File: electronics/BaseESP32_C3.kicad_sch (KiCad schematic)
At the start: 21 parts, among them J10 Conn_01x06, J11 Boot jumper, SW1 SW_Push, U1 ESP32-C3-MINI-1-N4

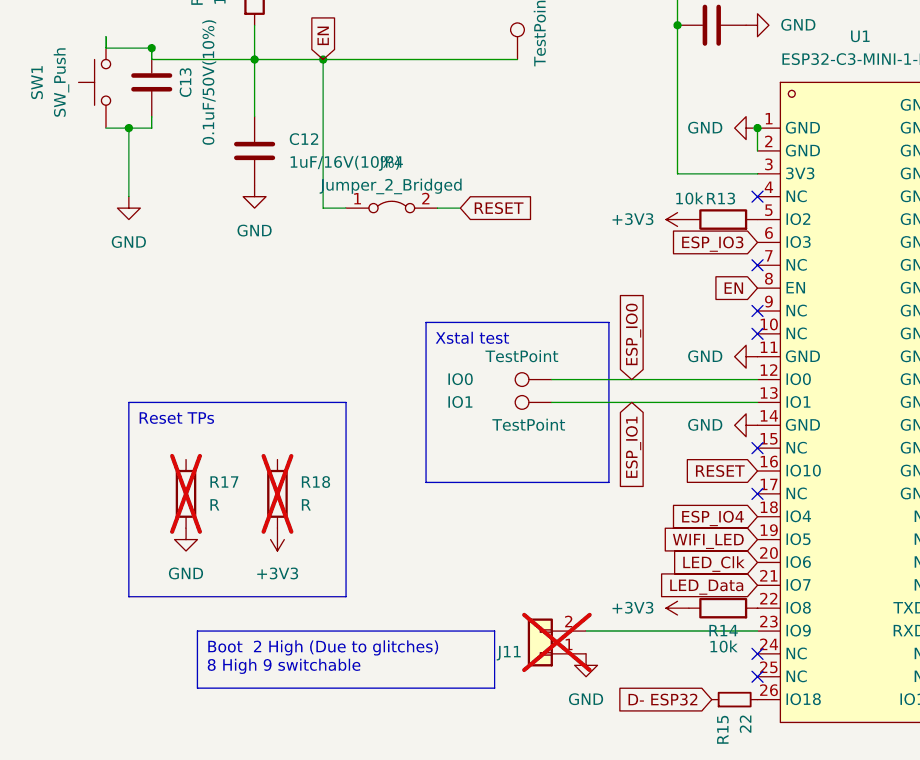
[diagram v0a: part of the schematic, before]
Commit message: components placed and tracks routed, needs silkscreen, drc and checking
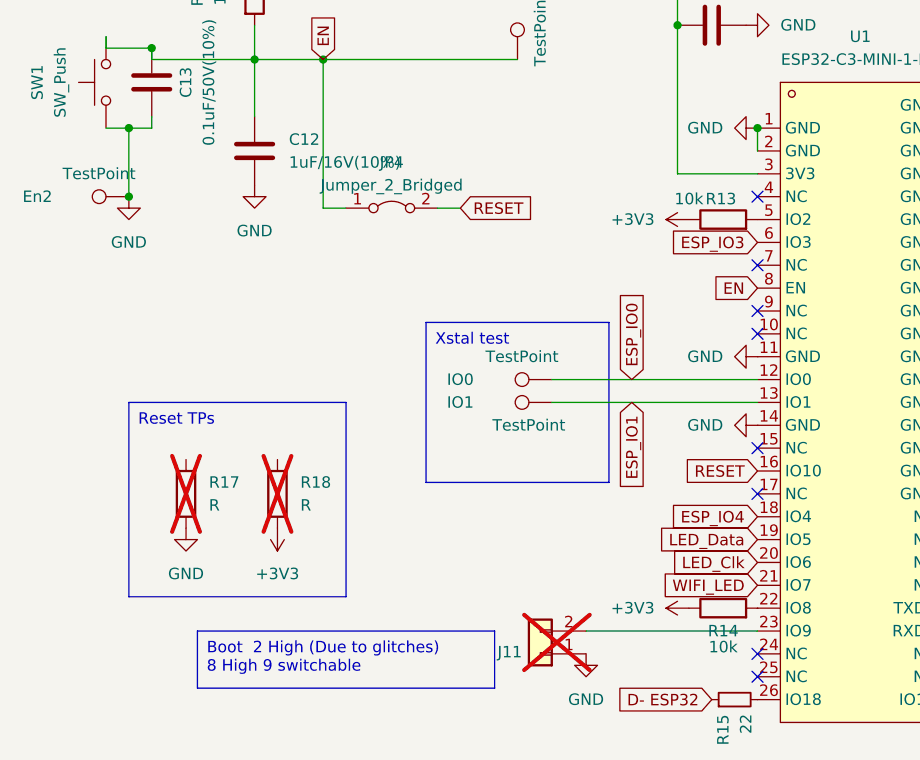
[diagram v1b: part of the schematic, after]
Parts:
- added En2: TestPoint, TestPoint:TestPoint_Pad_D2.5mm, symbol Connector:TestPoint
- R12, R13, R14, R15, R16: footprint Resistor_SMD:R_0603_1608Metric_Pad0.98x0.95mm_HandSolder -> Resistor_SMD:R_0402_1005Metric_Pad0.72x0.64mm_HandSolder
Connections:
- net GND: now also En2.1
- net LED_Data: now also U1.19 (IO5); no longer U1.21 (IO7)
- net WIFI_LED: now also U1.21 (IO7); no longer U1.19 (IO5)
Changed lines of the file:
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@@
 	)
 	(junction
+		(at 78.74 96.52)
+		(diameter 0)
+		(color 0 0 0 0)
+	)
+	(junction
 		(at 148.59 88.9)
 		(diameter 0)
@@
 		)
 	)
-	(global_label "LED_Data"
-		(shape input)
-		(at 148.59 139.7 180)
-		(fields_autoplaced yes)
-		(effects
-			(font
-				(size 1.27 1.27)
-			)
-			(justify right)
-		)
-		(property "Intersheetrefs" "${INTERSHEET_REFS}"
-			(at 137.5506 139.7 0)
-			(effects
-				(font
-					(size 1.27 1.27)
-				)
-				(justify right)
-				(hide yes)
-			)
-		)
-	)
 	(global_label "Tx"
 		(shape input)
@@
 		)
 	)
-	(global_label "WIFI_LED"
+	(global_label "D+ ESP32"
 		(shape input)
-		(at 148.59 134.62 180)
+		(at 176.53 152.4 0)
 		(fields_autoplaced yes)
 		(effects
@@
 				(size 1.27 1.27)
 			)
-			(justify right)
+			(justify left)
 		)
 		(property "Intersheetrefs" "${INTERSHEET_REFS}"
-			(at 138.0947 134.62 0)
+			(at 188.7185 152.4 0)
 			(effects
 				(font
 					(size 1.27 1.27)
 				)
-				(justify right)
+				(justify left)
 				(hide yes)
 			)
 		)
 	)
-	(global_label "D+ ESP32"
+	(global_label "EN"
 		(shape input)
-		(at 176.53 152.4 0)
+		(at 100.33 81.28 90)
 		(fields_autoplaced yes)
 		(effects
@@
 		)
 		(property "Intersheetrefs" "${INTERSHEET_REFS}"
-			(at 188.7185 152.4 0)
+			(at 100.33 76.4695 90)
 			(effects
 				(font
@@
 		)
 	)
-	(global_label "EN"
+	(global_label "WIFI_LED"
 		(shape input)
-		(at 100.33 81.28 90)
+		(at 148.59 139.7 180)
 		(fields_autoplaced yes)
 		(effects
@@
 				(size 1.27 1.27)
 			)
-			(justify left)
+			(justify right)
 		)
 		(property "Intersheetrefs" "${INTERSHEET_REFS}"
-			(at 100.33 76.4695 90)
+			(at 138.0947 139.7 0)
 			(effects
 				(font
 					(size 1.27 1.27)
 				)
-				(justify left)
+				(justify right)
 				(hide yes)
 			)
@@
 		)
 	)
+	(global_label "LED_Data"
+		(shape input)
+		(at 148.59 134.62 180)
+		(fields_autoplaced yes)
+		(effects
+			(font
+				(size 1.27 1.27)
+			)
+			(justify right)
+		)
+		(property "Intersheetrefs" "${INTERSHEET_REFS}"
+			(at 137.5506 134.62 0)
+			(effects
+				(font
+					(size 1.27 1.27)
+				)
+				(justify right)
+				(hide yes)
+			)
+		)
+	)
 	(symbol
 		(lib_id "power:GND")
@@
 			)
 		)
-		(property "Footprint" "Resistor_SMD:R_0603_1608Metric_Pad0.98x0.95mm_HandSolder"
+		(property "Footprint" "Resistor_SMD:R_0402_1005Metric_Pad0.72x0.64mm_HandSolder"
 			(at 173.99 152.4 0)
 			(effects
@@
 			)
 		)
-		(property "Footprint" "Resistor_SMD:R_0603_1608Metric_Pad0.98x0.95mm_HandSolder"
+		(property "Footprint" "Resistor_SMD:R_0402_1005Metric_Pad0.72x0.64mm_HandSolder"
 			(at 144.78 100.838 90)
 			(effects
@@
 	)
 	(symbol
+		(lib_id "Connector:TestPoint")
+		(at 78.74 96.52 90)
+		(unit 1)
+		(exclude_from_sim no)
+		(in_bom yes)
+		(on_board yes)
+		(dnp no)
+		(property "Reference" "En2"
+			(at 68.58 96.52 90)
+			(effects
+				(font
+					(size 1.27 1.27)
+				)
+			)
+		)
+		(property "Value" "TestPoint"
+			(at 75.438 93.98 90)
+			(effects
+				(font
+					(size 1.27 1.27)
+				)
+			)
+		)
+		(property "Footprint" "TestPoint:TestPoint_Pad_D2.5mm"
+			(at 78.74 91.44 0)
+			(effects
+				(font
+					(size 1.27 1.27)
+				)
+				(hide yes)
+			)
+		)
+		(property "Datasheet" "~"
+			(at 78.74 91.44 0)
+			(effects
+				(font
+					(size 1.27 1.27)
+				)
+				(hide yes)
+			)
+		)
+		(property "Description" ""
+			(at 78.74 96.52 0)
+			(effects
+				(font
+					(size 1.27 1.27)
+				)
+				(hide yes)
+			)
+		)
+		(pin "1"
+		)
+		(instances
+			(project "MyBikesGotLED"
+				(path "/ea56fda8-6f8e-4826-a040-5c9b3e8e5cfa/0b0225ac-45b5-41c8-a760-6f29a7cb924b"
+					(reference "En2")
+					(unit 1)
+				)
+			)
+		)
+	)
+	(symbol
 		(lib_id "power:GND")
 		(at 85.09 133.35 0)
@@
 			)
 		)
-		(property "Footprint" "Resistor_SMD:R_0603_1608Metric_Pad0.98x0.95mm_HandSolder"
+		(property "Footprint" "Resistor_SMD:R_0402_1005Metric_Pad0.72x0.64mm_HandSolder"
 			(at 197.358 121.92 90)
 			(effects
@@
 			)
 		)
-		(property "Footprint" "Resistor_SMD:R_0603_1608Metric_Pad0.98x0.95mm_HandSolder"
+		(property "Footprint" "Resistor_SMD:R_0402_1005Metric_Pad0.72x0.64mm_HandSolder"
 			(at 146.05 152.4 0)
 			(effects
@@
 			)
 		)
-		(property "Footprint" "Resistor_SMD:R_0603_1608Metric_Pad0.98x0.95mm_HandSolder"
+		(property "Footprint" "Resistor_SMD:R_0402_1005Metric_Pad0.72x0.64mm_HandSolder"
 			(at 144.78 144.018 90)
 			(effects

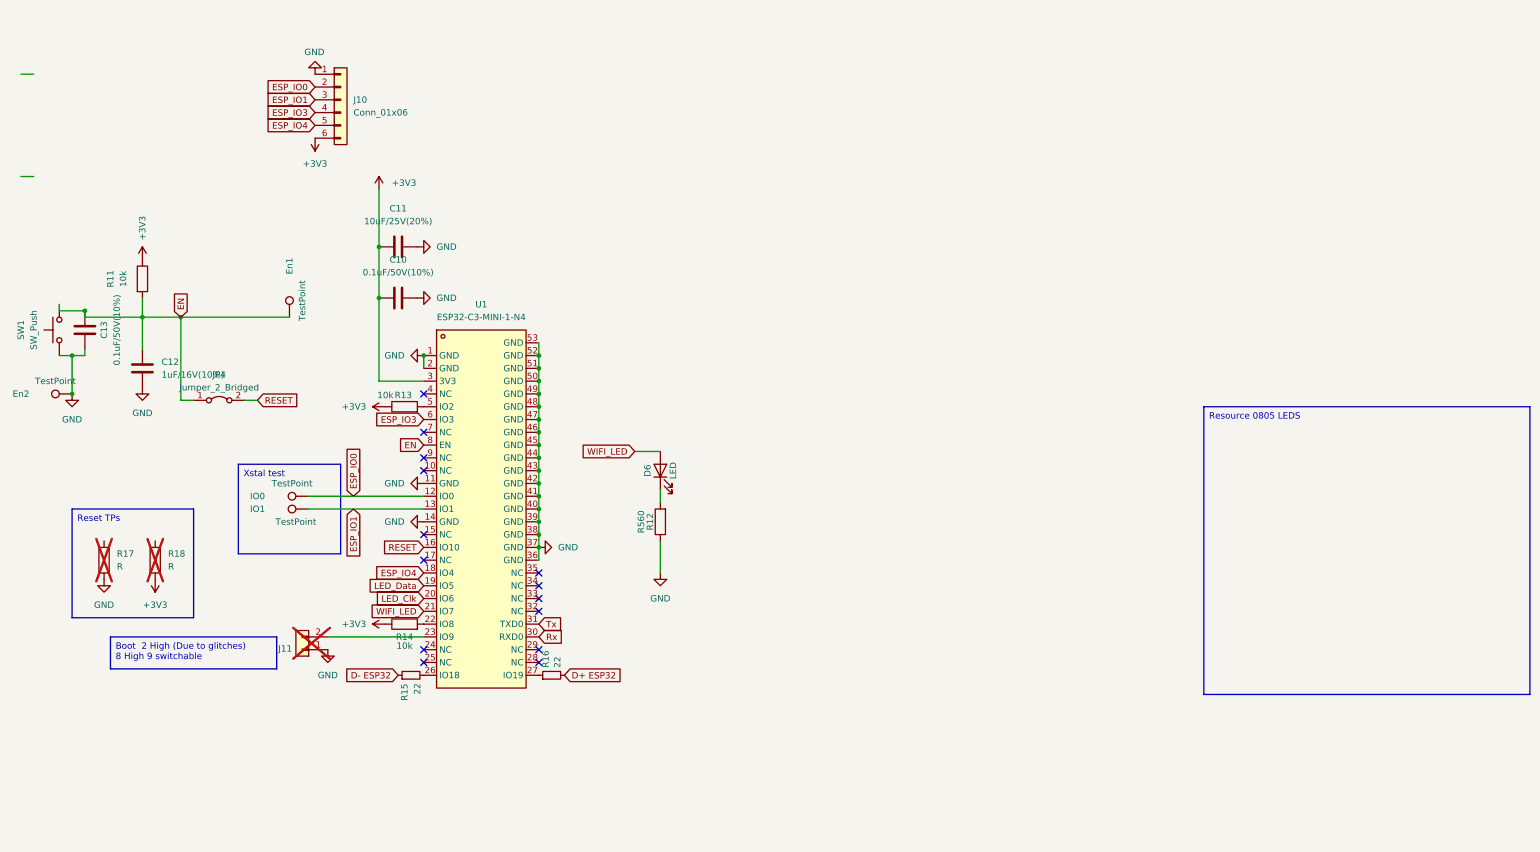
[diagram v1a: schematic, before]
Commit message: Finished silkscreen, added new LSCS codes to reflect current JLC stock
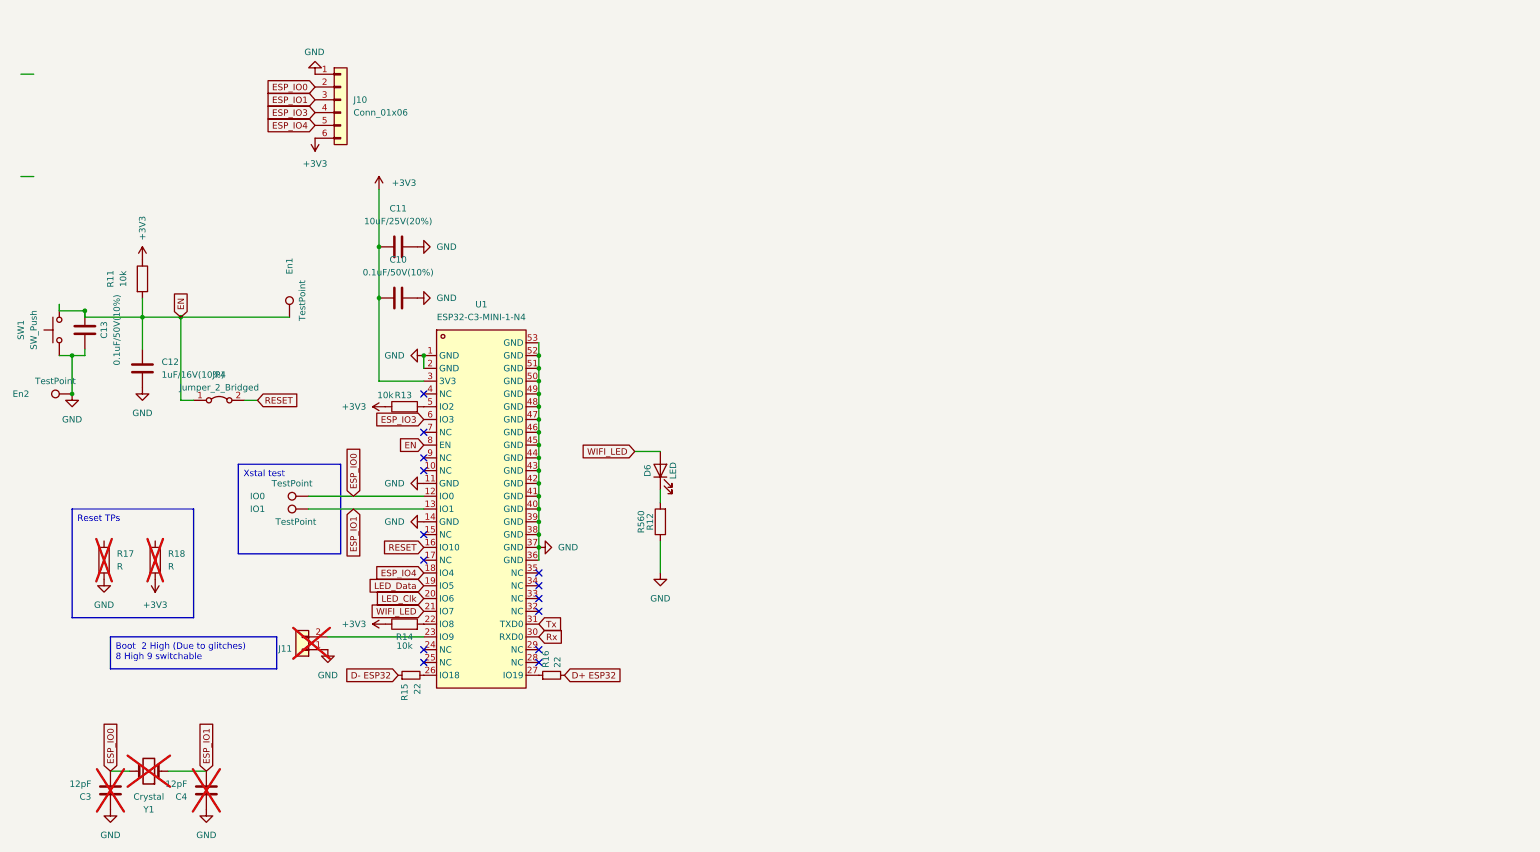
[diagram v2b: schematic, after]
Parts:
- added C3, C4: 12pF, Capacitor_SMD:C_0603_1608Metric_Pad1.08x0.95mm_HandSolder, symbol Device:C
- added Y1: Crystal, Crystal:Crystal_SMD_3215-2Pin_3.2x1.5mm, symbol Device:Crystal
- C11: LCSC Stock https://www.lcsc.com/product-detail/Multilayer-Ceramic-Capa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 -> (none)
- D6: LCSC C497935 -> C601686; LCSC Stock https://www.lcsc.com/product-detail/LED-Indication-Discrete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 -> (none)
- R11: LCSC C862388 -> C95204; LCSC Stock https://www.lcsc.com/product-detail/Chip-span-style-backgro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 -> (none)
- R12: LCSC C5455512 -> C20573; LCSC Stock https://www.lcsc.com/product-detail/Chip-span-style-backgro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 -> (none)
- R13, R14: LCSC C862388 -> C2073569; LCSC Stock https://www.lcsc.com/product-detail/Chip-span-style-backgro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 -> (none)
- R15, R16: LCSC C860239 -> C5139642; LCSC Stock https://www.lcsc.com/product-detail/Chip-span-style-backgro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 -> (none)
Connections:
- net ESP_IO0: now also C3.2, Y1.2
- net ESP_IO1: now also C4.2, Y1.1
- net GND: now also C3.1, C4.1

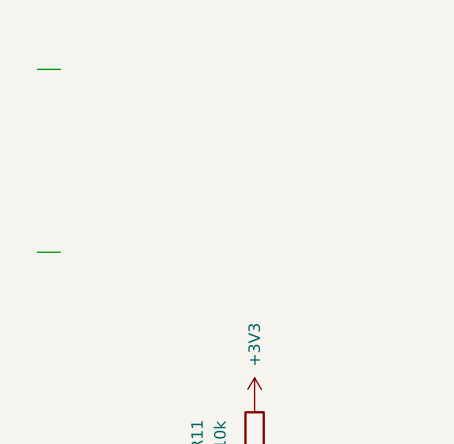
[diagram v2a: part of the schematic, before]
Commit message: Move R12 silkscreen; tidy keepout area copper near the C3.  Part of #29
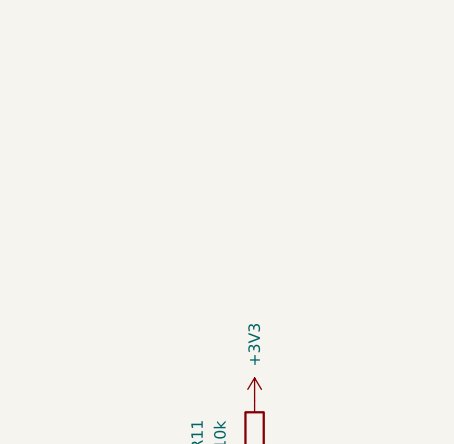
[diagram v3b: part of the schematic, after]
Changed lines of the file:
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@@
-	(wire
-		(pts
-			(xy 68.58 33.02) (xy 71.12 33.02)
-		)
-		(stroke
-			(width 0)
-			(type default)
-		)
-	)
 	(wire
 		(pts
@@
 		)
 		(stroke
-			(width 0)
-			(type default)
-		)
-	)
-	(wire
-		(pts
-			(xy 71.12 53.34) (xy 68.58 53.34)
-		)
-		(stroke

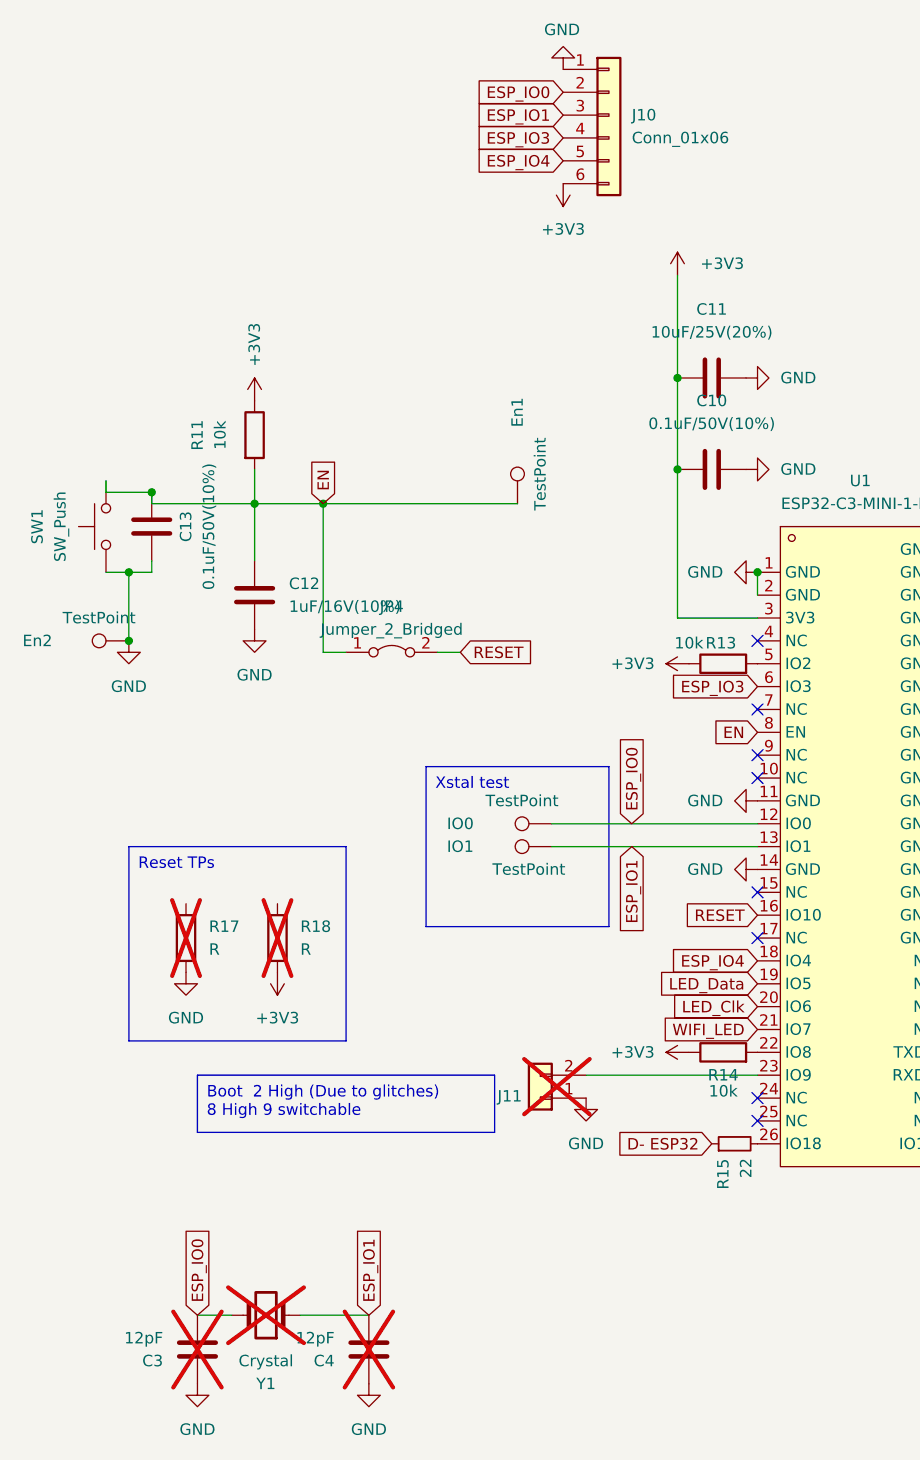
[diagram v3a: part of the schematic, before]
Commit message: v2.1 pcb tweaks from #29. Silkscreen, LED spec and the keep alive power led outstanding
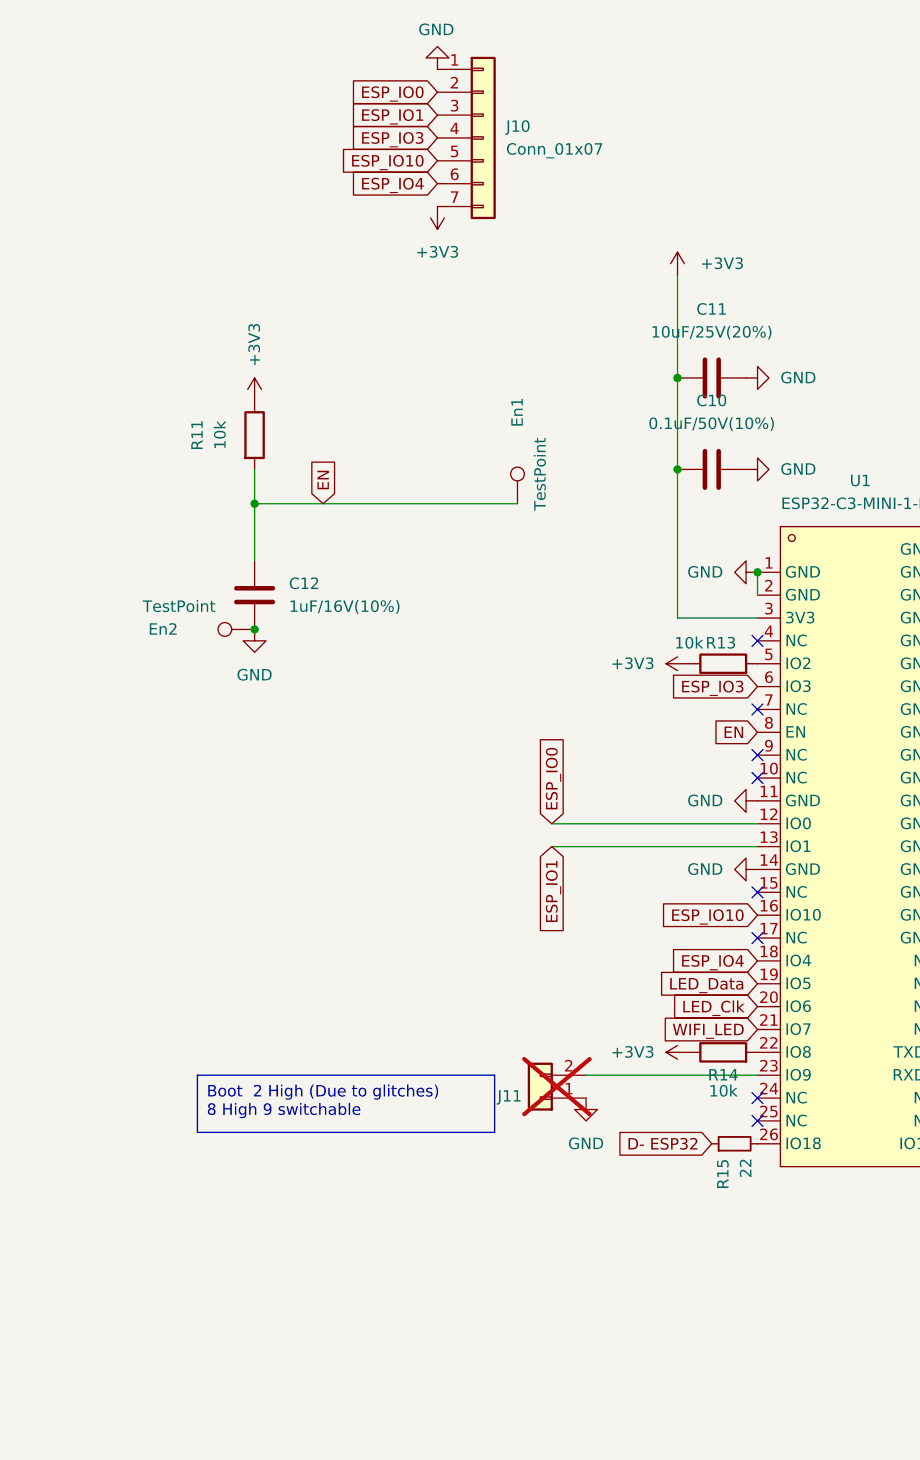
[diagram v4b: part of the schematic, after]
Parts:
- removed C13: 0.1uF/50V(10%), Capacitor_SMD:C_0603_1608Metric_Pad1.08x0.95mm_HandSolder, symbol Device:C
- removed C3, C4: 12pF, Capacitor_SMD:C_0603_1608Metric_Pad1.08x0.95mm_HandSolder, symbol Device:C
- removed IO0, IO1: TestPoint, TestPoint:TestPoint_Pad_D2.5mm, symbol Connector:TestPoint
- removed J10: Conn_01x06, Connector_PinSocket_2.54mm:PinSocket_1x06_P2.54mm_Vertical, symbol Connector_Generic:Conn_01x06
- removed JP4: Jumper_2_Bridged, Jumper:SolderJumper-2_P1.3mm_Bridged_RoundedPad1.0x1.5mm, symbol Jumper:Jumper_2_Bridged
- removed R17, R18: R, Resistor_SMD:R_0805_2012Metric, symbol Device:R
- removed SW1: SW_Push, Button_Switch_SMD:SW_Push_1P1T_NO_6x6mm_H9.5mm, symbol Switch:SW_Push
- removed Y1: Crystal, Crystal:Crystal_SMD_3215-2Pin_3.2x1.5mm, symbol Device:Crystal
- added J10: Conn_01x07, Connector_PinHeader_2.54mm:PinHeader_1x07_P2.54mm_Vertical, symbol Connector_Generic:Conn_01x07
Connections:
- net +3V3: now also J10.7 (Pin_7)
- net ESP_IO0: now also J10.2 (Pin_2)
- net ESP_IO1: now also J10.3 (Pin_3)
- net ESP_IO3: now also J10.4 (Pin_4)
- net ESP_IO4: now also J10.6 (Pin_6)
- net GND: now also J10.1 (Pin_1)
- net RESET renamed ESP_IO10
- net ESP_IO10: now also J10.5 (Pin_5)
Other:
- moved on the sheet: En2
